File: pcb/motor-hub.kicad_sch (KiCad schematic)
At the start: 20 parts, among them J11 Screw_Terminal_01x10, U7 STM32G431CBUx, U8 74HC595, Y1 16MHz

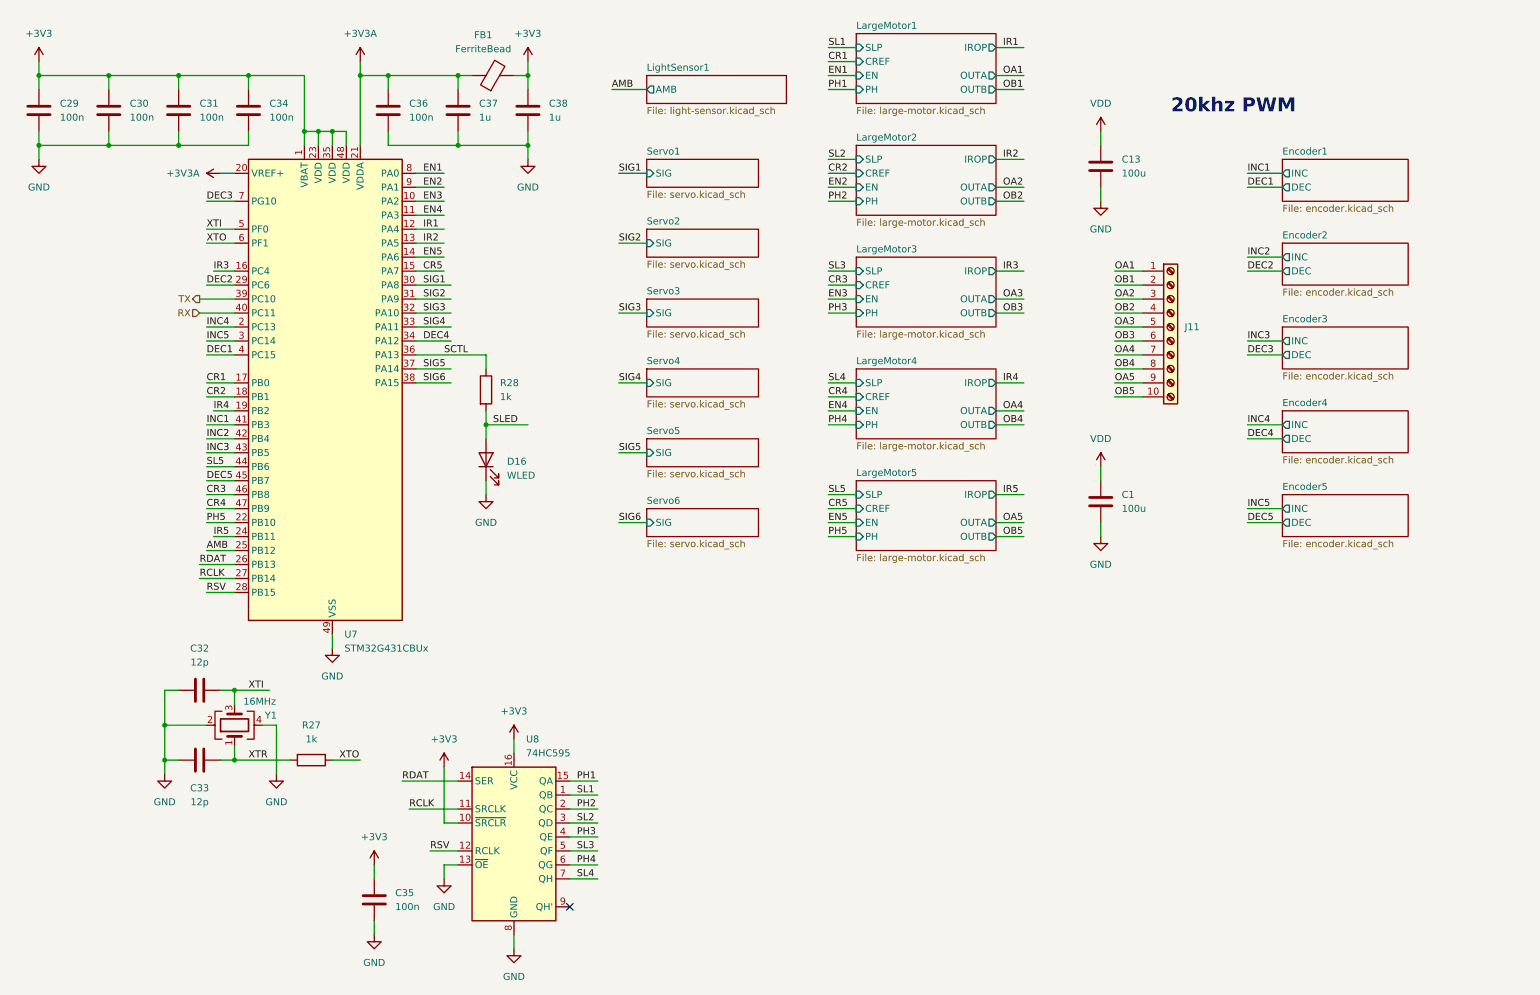
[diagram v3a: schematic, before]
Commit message: Finish first draft schematic
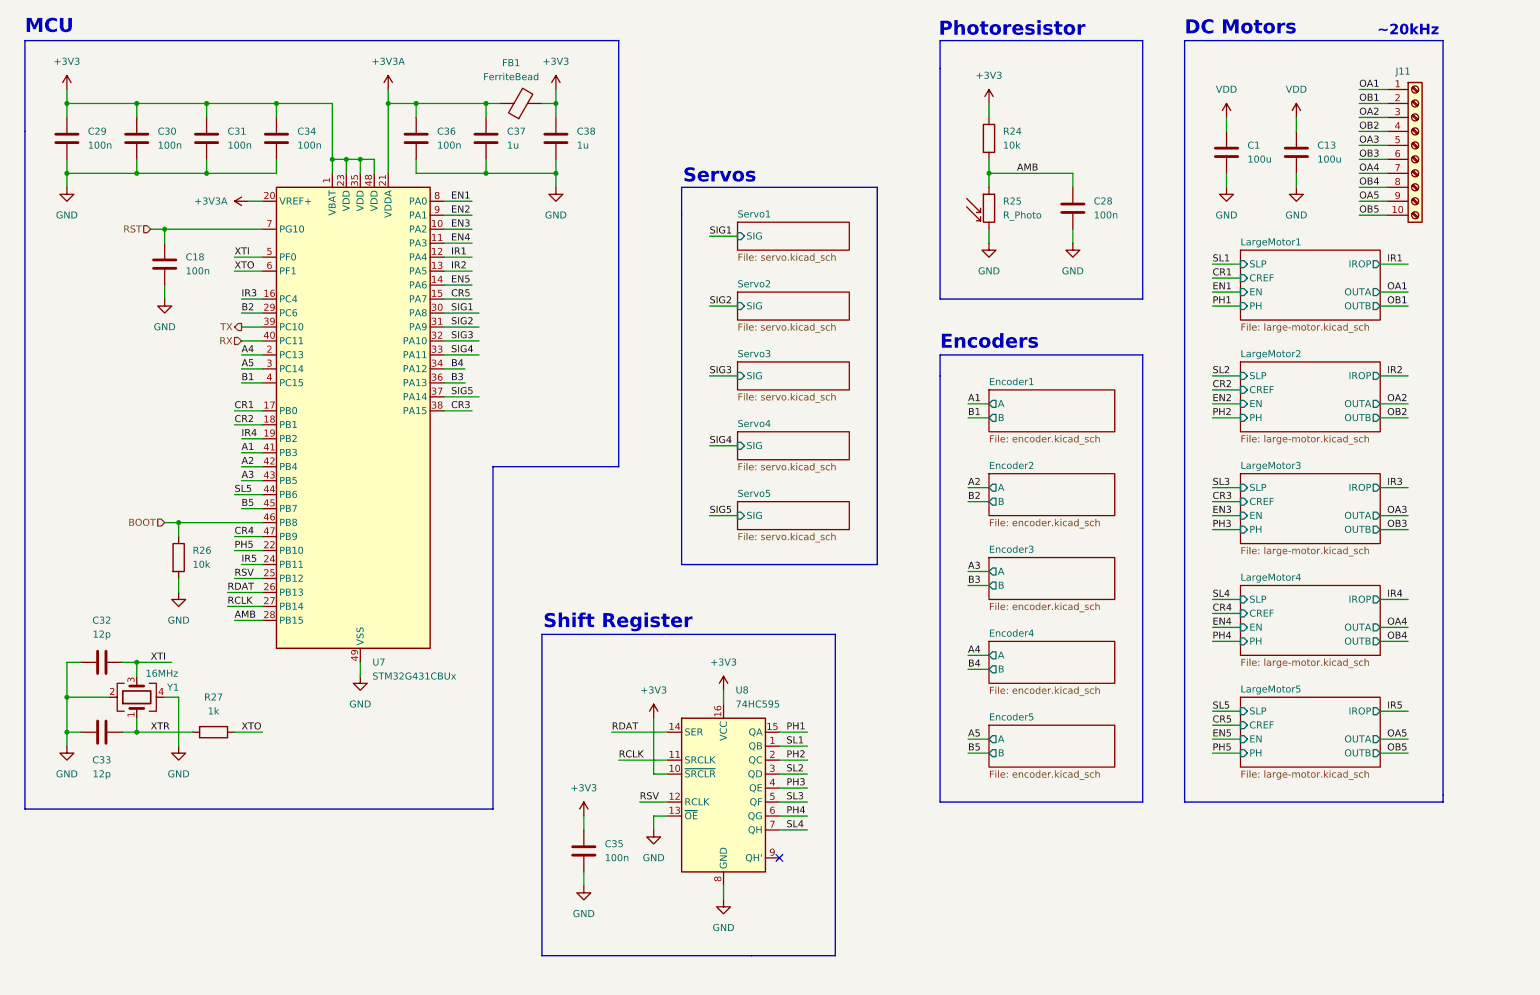
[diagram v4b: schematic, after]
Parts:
- removed D16: WLED, LED_SMD:LED_0603_1608Metric, symbol Device:LED
- removed R28: 1k, Resistor_SMD:R_0402_1005Metric, symbol Device:R
- added C18, C28: 100n, Capacitor_SMD:C_0402_1005Metric, symbol Device:C
- added R24, R26: 10k, Resistor_SMD:R_0402_1005Metric, symbol Device:R
- added R25: R_Photo, Resistor_SMD:R_1210_3225Metric, symbol Device:R_Photo
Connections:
- net SIG6 is gone; now on net CR3: U7.38 (PA15)
- net +3V3: now also R24.1
- net AMB: now also U7.28 (PB15), C28.1, R24.2, R25.1; no longer U7.25 (PB12)
- net CR3: no longer U7.46 (PB8)
- net GND: now also C18.2, C28.2, R25.2, R26.2
- net RSV: now also U7.25 (PB12); no longer U7.28 (PB15)
- net DEC1 renamed B1
- net DEC2 renamed B2
- net DEC3 renamed RST
- net RST: now also C18.1
- net DEC4 renamed B4
- net DEC5 renamed B5
- net INC1 renamed A1
- net INC2 renamed A2
- net INC3 renamed A3
- net INC4 renamed A4
- net INC5 renamed A5
- net SCTL renamed B3
- new net BOOT: R26.1, U7.46 (PB8)
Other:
- removed sheet LightSensor1
- removed sheet Servo6
- sheet Encoder1 ports: added A, B; removed DEC, INC
- sheet Encoder2 ports: added A, B; removed DEC, INC
- sheet Encoder3 ports: added A, B; removed DEC, INC
- sheet Encoder4 ports: added A, B; removed DEC, INC
- sheet Encoder5 ports: added A, B; removed DEC, INC
- note added: "DC Motors"
- note added: "Encoders"
- note added: "MCU"
- note added: "Photoresistor"
- note added: "Servos"
- note added: "Shift Register"
- note added: "~20kHz"
- note removed: "20khz PWM"
- moved on the sheet: C1, C13, C29, C30, C31, C32, C33, C34, C35, C36, C37, C38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

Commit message: Save progress
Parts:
- removed C13: 100u, Capacitor_SMD:C_Elec_8x6.2, symbol Device:C
- added J10, J12, J13, J19, J20: Screw_Terminal_01x02, symbol Connector:Screw_Terminal_01x02
- added R55: 10k, Resistor_SMD:R_0402_1005Metric, symbol Device:R
- added SW1, SW2: SW_Push, Footprints:TS-1088, symbol Switch:SW_Push
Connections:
- net +3V3: now also R55.1, SW2.1
- net GND: now also SW1.1
- net RST: now also R55.2, SW1.2
- net BOOT renamed BT0
- net BT0: now also SW2.2
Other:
- moved on the sheet: C1, C18, J11

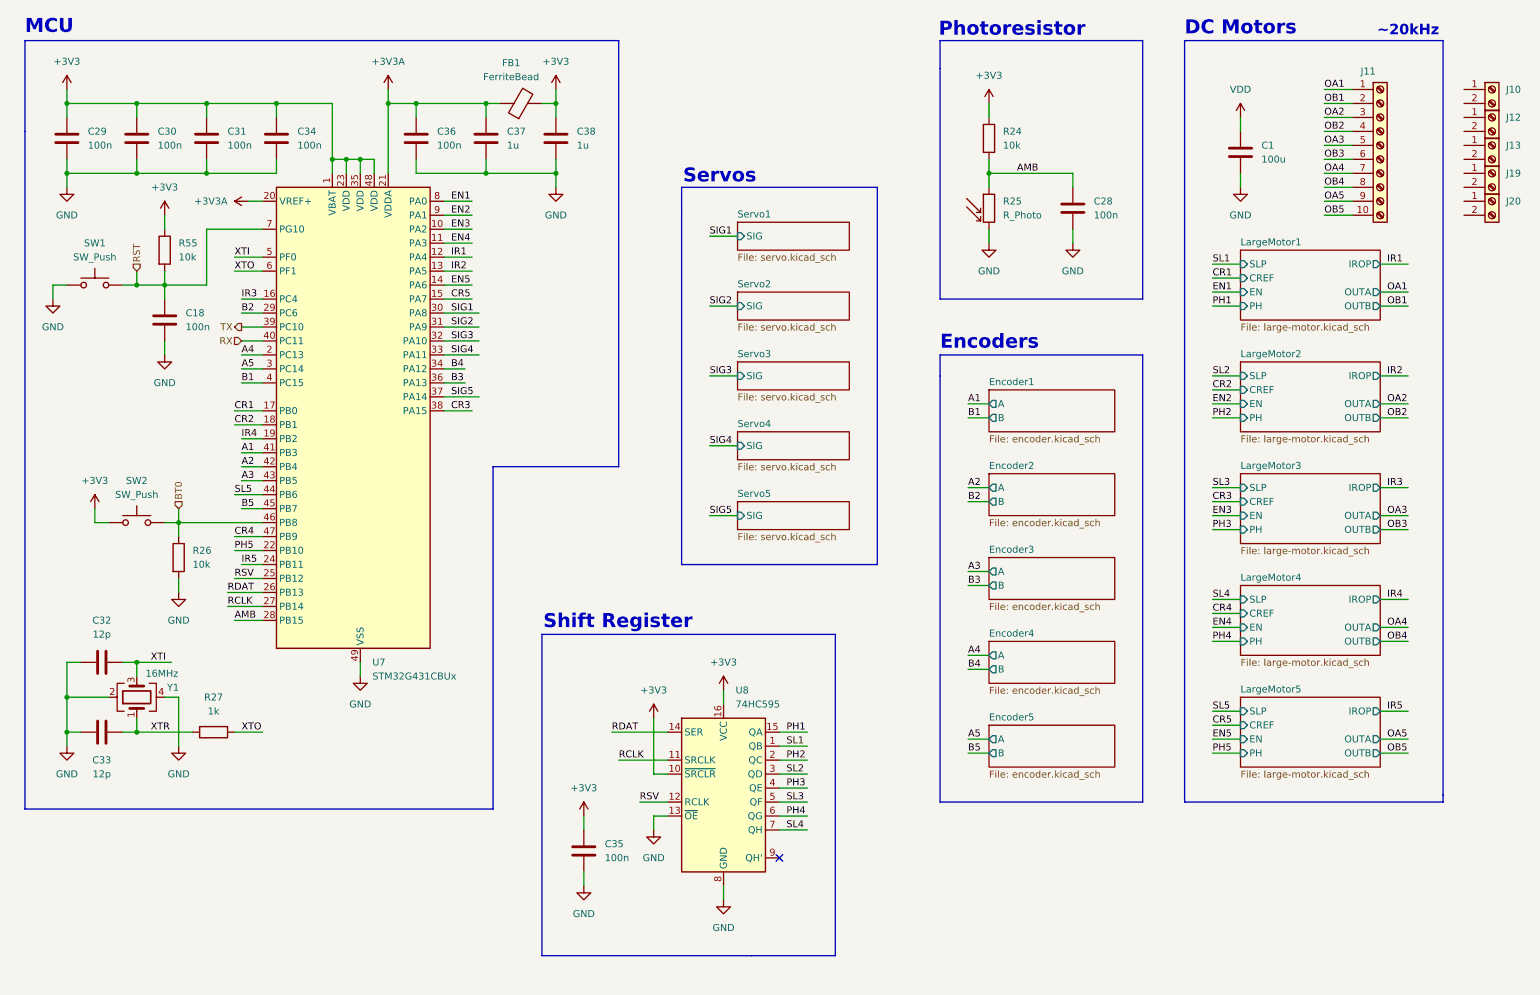
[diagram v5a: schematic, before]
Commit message: Finish schematic
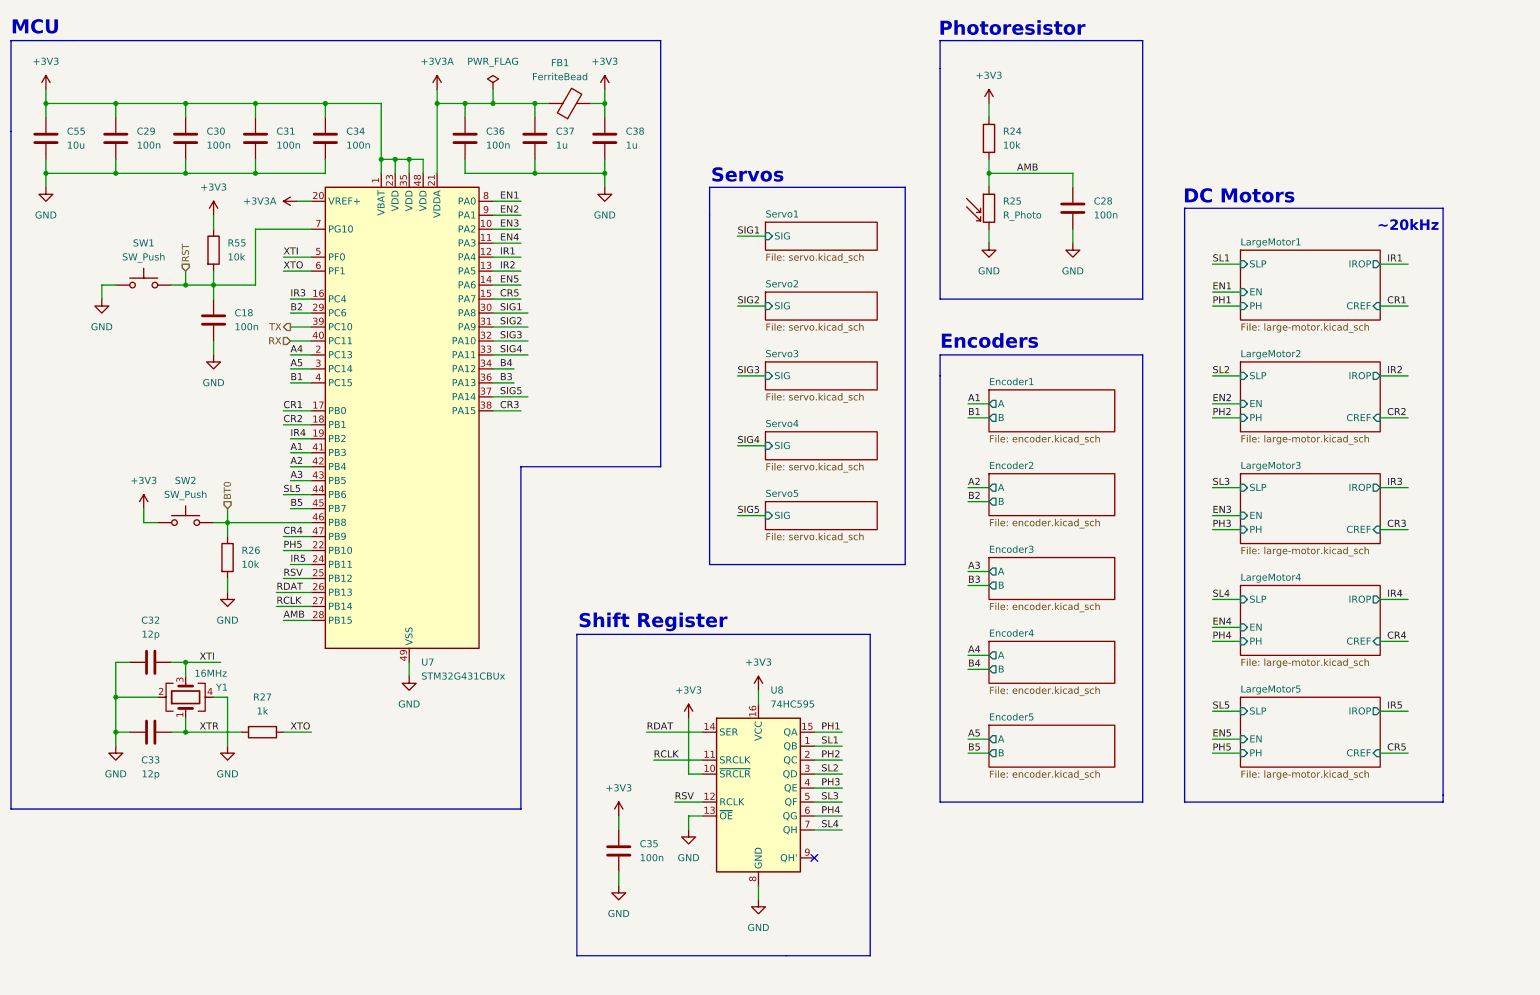
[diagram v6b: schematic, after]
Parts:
- removed C1: 100u, Capacitor_SMD:C_Elec_8x6.2, symbol Device:C
- removed J10, J12, J13, J19, J20: Screw_Terminal_01x02, symbol Connector:Screw_Terminal_01x02
- removed J11: Screw_Terminal_01x10, TerminalBlock_Phoenix:TerminalBlock_Phoenix_MKDS-1,5-10_1x10_P5.00mm_Horizontal, symbol Connector:Screw_Terminal_01x10
- added C55: 10u, Capacitor_SMD:C_0402_1005Metric, symbol Device:C
- U8: LCSC C110383 -> C5947
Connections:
- net +3V3: now also C55.1
- net GND: now also C55.2
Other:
- sheet LargeMotor1 ports: added none; removed OUTA, OUTB
- sheet LargeMotor2 ports: added none; removed OUTA, OUTB
- sheet LargeMotor3 ports: added none; removed OUTA, OUTB
- sheet LargeMotor4 ports: added none; removed OUTA, OUTB
- sheet LargeMotor5 ports: added none; removed OUTA, OUTB
- moved on the sheet: C18, C29, C30, C31, C32, C33, C34, C35, C36, C37, C38, FB1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

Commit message: Start wiring
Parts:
- added J10: Conn_ARM_SWD_TagConnect_TC2030-NL, Connector:Tag-Connect_TC2030-IDC-NL_2x03_P1.27mm_Vertical, symbol Connector:Conn_ARM_SWD_TagConnect_TC2030-NL
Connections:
- net +3V3: now also J10.1 (VCC)
- net B3: now also J10.2 (SWDIO)
- net GND: now also J10.5 (GND)
- net RST: now also J10.3 (~{RESET})
- net SIG5: now also J10.4 (SWCLK)
- no-connect marks 1 -> 2

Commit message: Save progress
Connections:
- net XTI: now also R27.1; no longer C32.2, Y1.3
- net XTO: now also C32.2, Y1.3; no longer R27.1
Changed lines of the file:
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@@
 		)
 	)
-	(label "XTO"
+	(label "XTI"
 		(at 68.58 147.32 0)
 		(fields_autoplaced yes)
@@
 		)
 	)
-	(label "XTI"
+	(label "XTO"
 		(at 52.07 134.62 0)
 		(fields_autoplaced yes)
